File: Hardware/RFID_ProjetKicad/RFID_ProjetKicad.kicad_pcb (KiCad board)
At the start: 2 copper layers, 152 x 72 mm, 36 parts, among them J1 TB0011-350-04GR, J2 TB0011-350-04GR, U1 XIAO-ESP32-C6-DIP, U2 RFID-RC522, U3 MAX3485CSA_T, X0 , X1 , X2 , X3 , X4 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

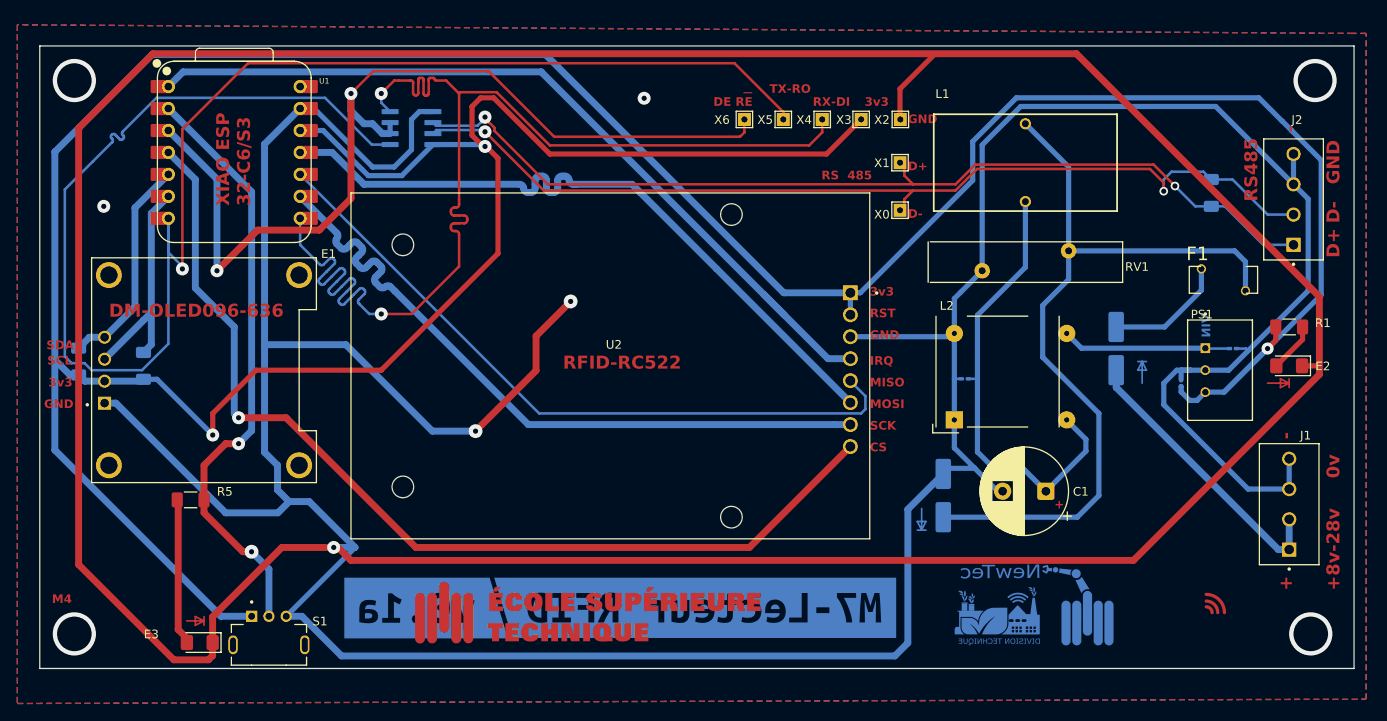
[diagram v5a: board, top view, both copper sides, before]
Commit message: Agrandissement des taille des pads
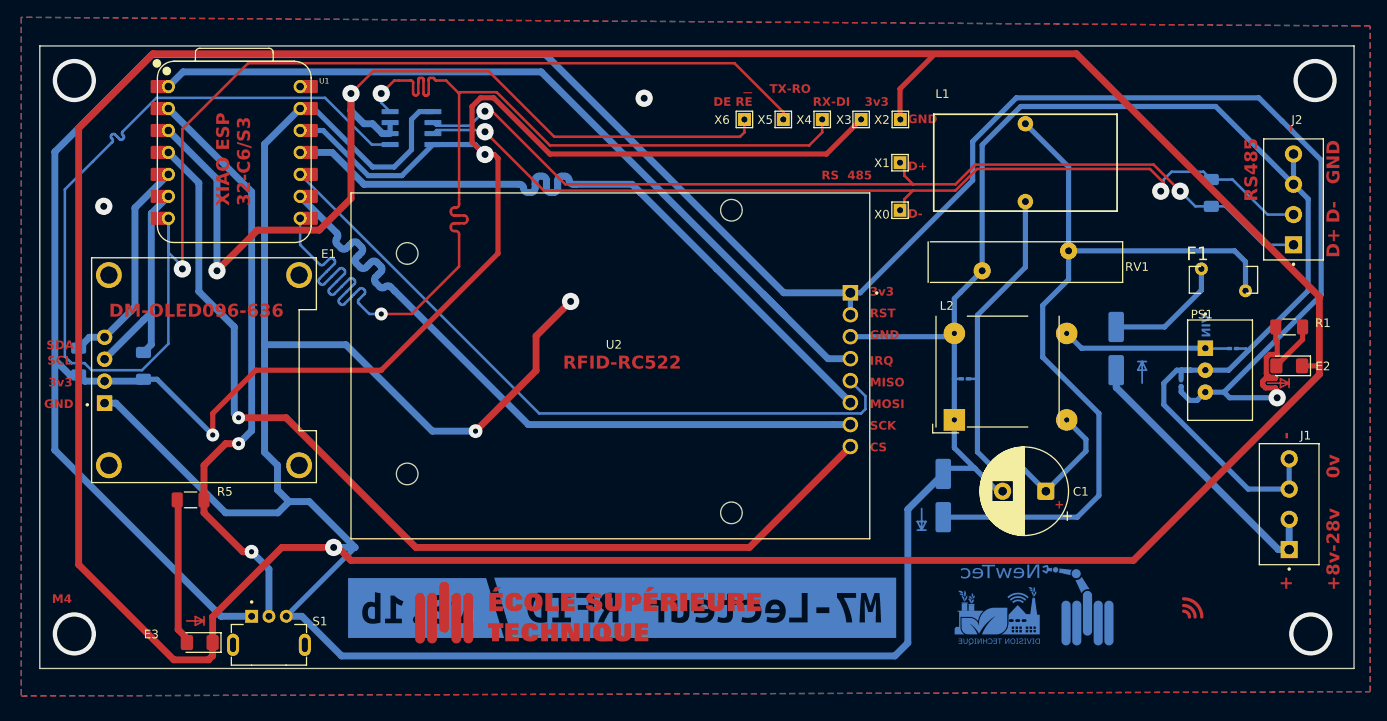
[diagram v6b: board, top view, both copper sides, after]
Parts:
- removed kibuzzard-69FBB450: G***, kibuzzard-69FBB450
- added kibuzzard-6A1B3F22: G***, kibuzzard-6A1B3F22, B.Cu at (116.3, 117.5)
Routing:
- net +3V3: track 452.2 -> 462.0 mm
- net /D+: track 112.4 -> 111.6 mm
- net /D-: track 111.9 -> 112.5 mm
